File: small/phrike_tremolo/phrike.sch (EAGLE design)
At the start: 38 parts, among them Q1 2N5457, Q2 2N3904, Q3 2N5457, Q4 2N5088

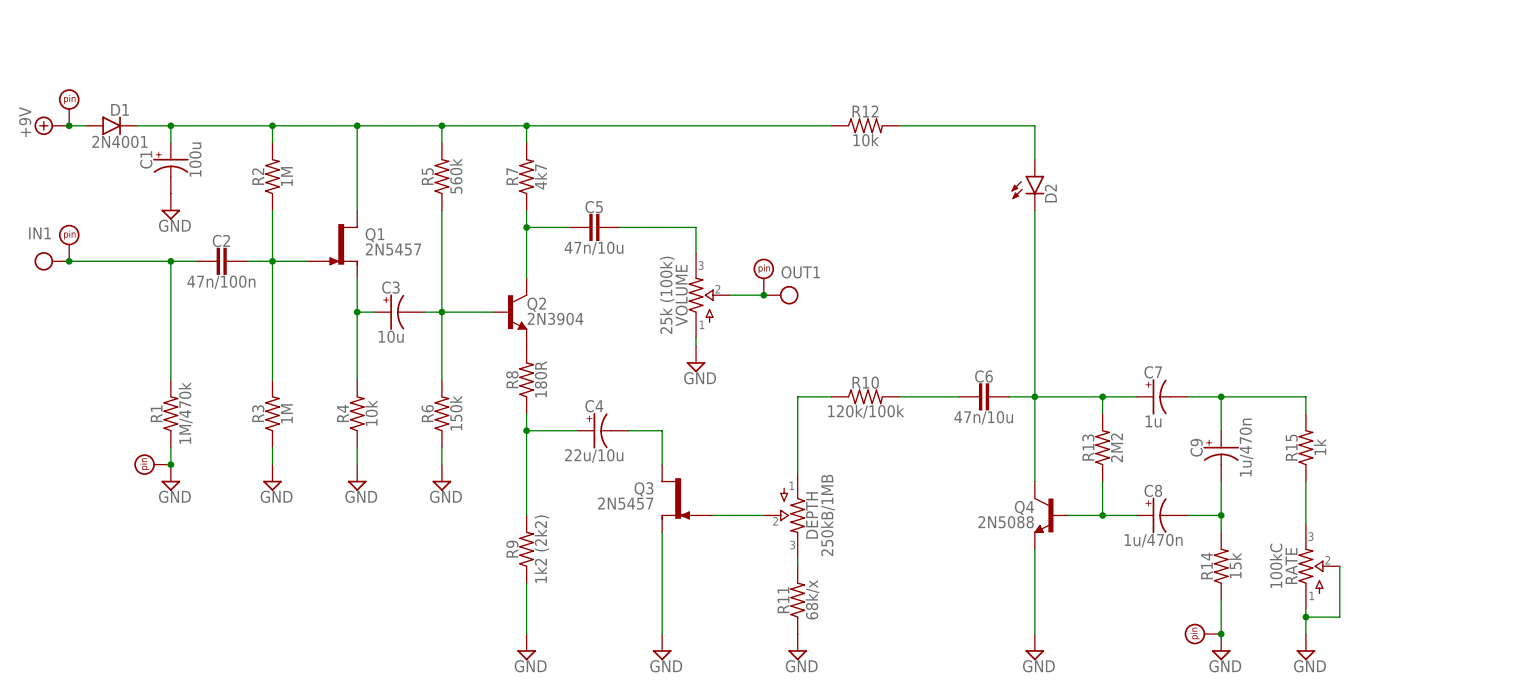
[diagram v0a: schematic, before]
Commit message: add EAGLE library, update 1590a chorus and tremolo, other minor edits
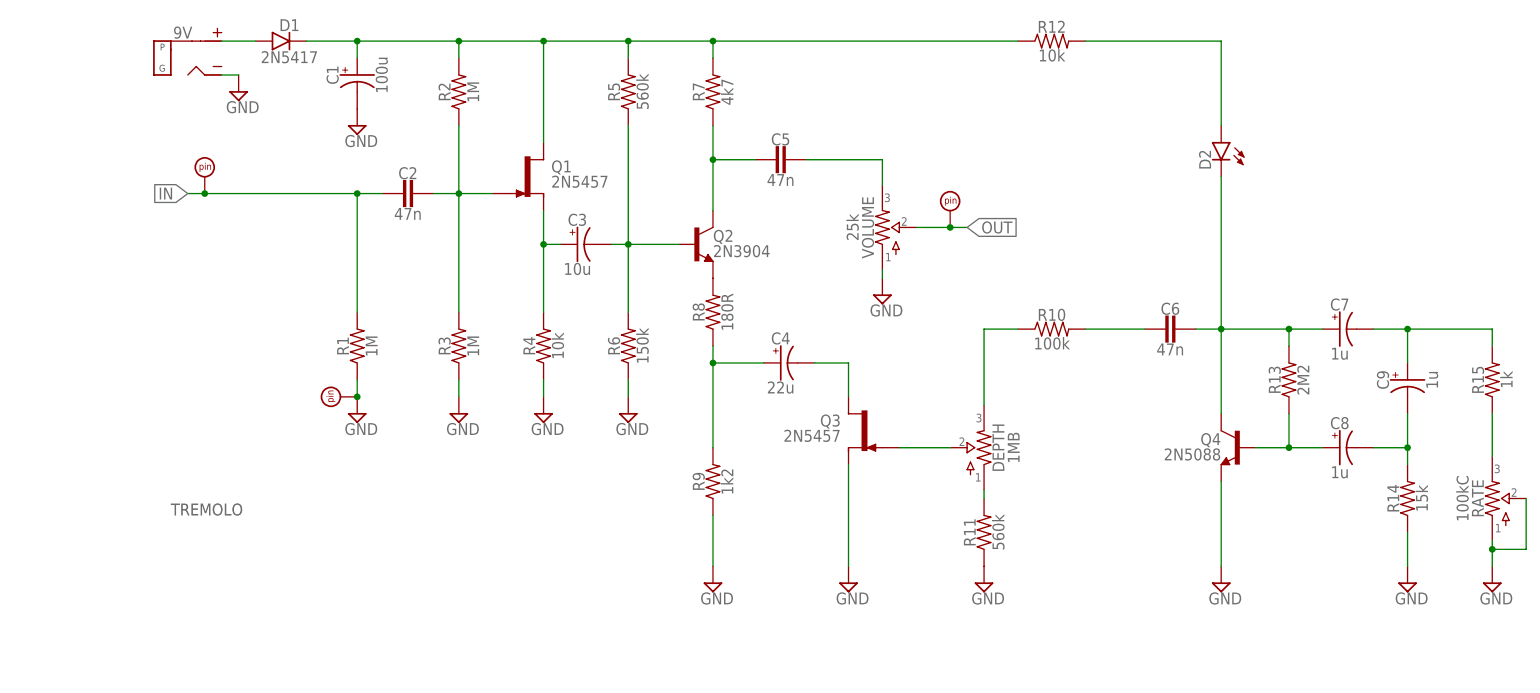
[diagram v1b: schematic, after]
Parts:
- removed PAD1, PAD2, PAD3: PADSQR, supply pins:PADSQR
- removed PAD4, PAD5: PADRND, supply pins:PADRND
- added 9V: DC_MONO, jacks:DC_MONO
- added GND: PADRND, supply pins:PADRND
- added IN, OUT: PADSQR, supply pins:PADSQR
- C1: device capacitors-elec:0501 -> capacitors-elec:0631
- C2: value 47n/100n -> 47n; device capacitors-film:CER/FILMBOX.1 -> capacitors-film:CER/FILM2
- C4: value 22u/10u -> 22u
- C5, C6: value 47n/10u -> 47n; device capacitors-film:CER/FILMBOX.1 -> capacitors-film:CER/FILM2
- C8, C9: value 1u/470n -> 1u
- D1: value 2N4001 -> 2N5417; device diodes:DO41.2 -> diodes:DO41.3
- DEPTH: value 250kB/1MB -> 1MB
- Q2: device transistors:2N3904 -> transistors:2N3904L2
- R1: value 1M/470k -> 1M
- R10: value 120k/100k -> 100k
- R11: value 68k/x -> 560k
- R9: value 1k2 (2k2) -> 1k2
- VOLUME: value 25k (100k) -> 25k
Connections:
- net +9V: now also 9V.TIP; no longer PAD1.P$1
- net GND: now also 9V.SLEEVE, GND.P$1; no longer PAD4.P$1, PAD5.P$1
- net IN: now also IN.P$1; no longer PAD2.P$1
- net N$11: now also DEPTH.3; no longer DEPTH.1
- net N$17: now also DEPTH.1; no longer DEPTH.3
- net OUT: now also OUT.P$1; no longer PAD3.P$1
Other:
- note added: "TREMOLO"
- moved on the sheet: C2, C3, C4, C5, C6, C7, C8, C9, D1, D2, DEPTH, Q1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
